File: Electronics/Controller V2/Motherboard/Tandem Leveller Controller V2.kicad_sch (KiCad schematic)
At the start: 6 parts, among them J8 776180-1, J9 776279-1

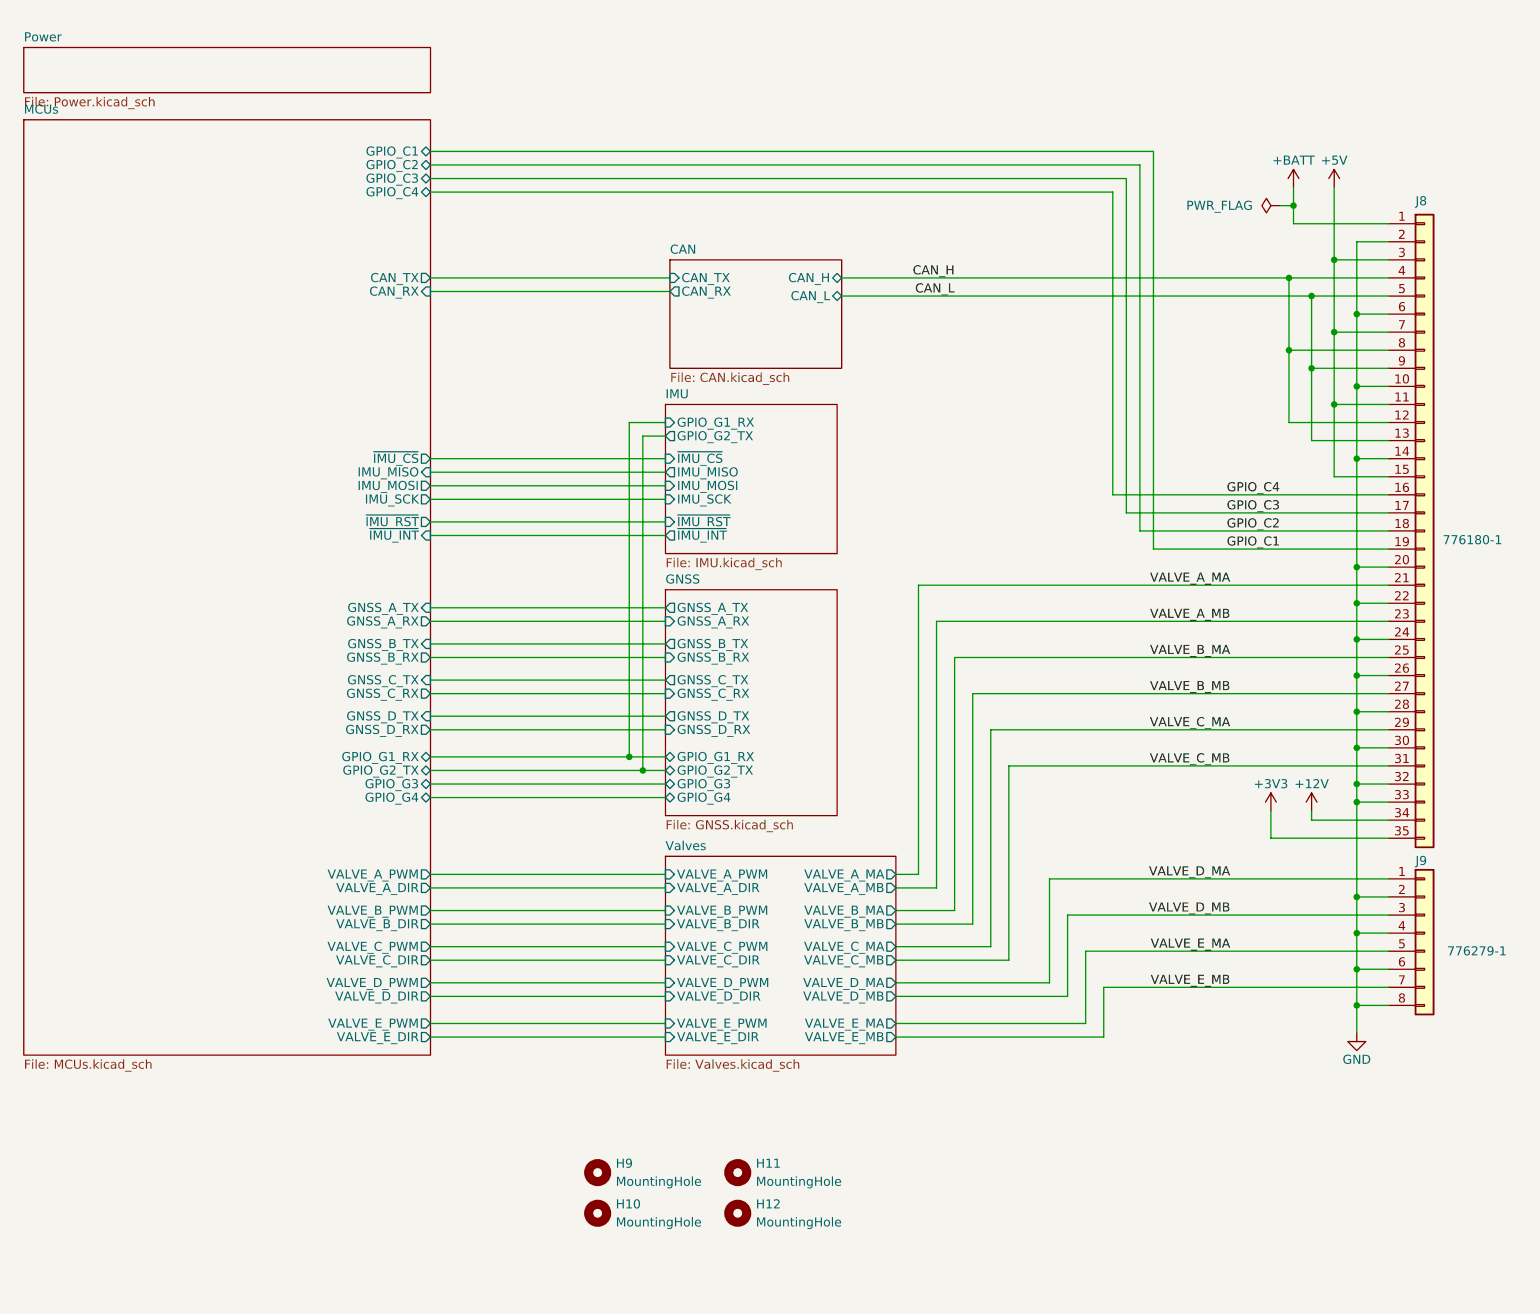
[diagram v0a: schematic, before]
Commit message: Added relay to control output of valve E.
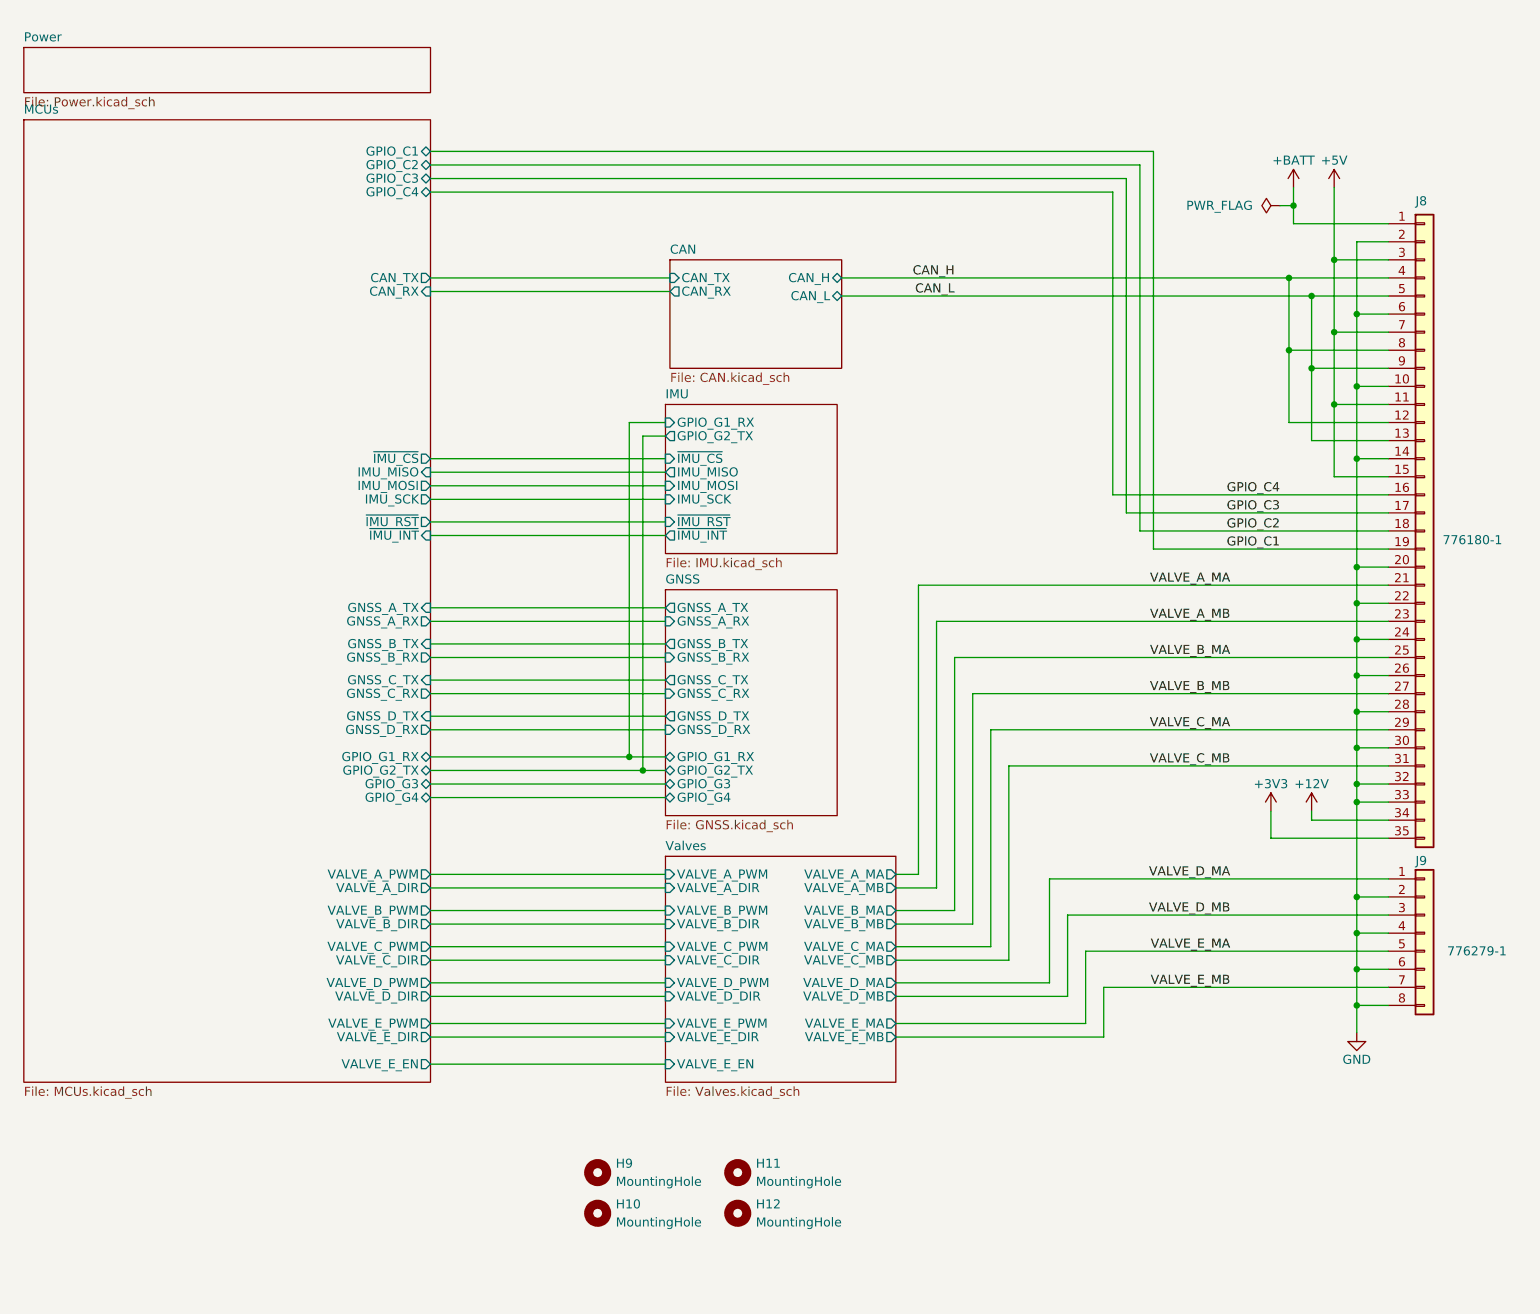
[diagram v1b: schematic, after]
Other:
- sheet MCUs ports: added VALVE_E_EN; removed none
- sheet Valves ports: added VALVE_E_EN; removed none
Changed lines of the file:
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@@
   (title_block
     (title "Tandem Leveller Controller")
-    (date "2026-02-09")
+    (date "2026-03-01")
     (rev "V2.0")
     (company "(C) andy@britishideas.com 2026")
@@
   )
   (wire (pts (xy 233.68 147.32) (xy 233.68 142.24))
+    (stroke (width 0) (type default))
+  )
+  (wire (pts (xy 103.505 160.655) (xy 136.525 160.655))
     (stroke (width 0) (type default))
   )
@@
     )
   )
-  (sheet (at 136.525 131.445) (size 32.385 27.94) (fields_autoplaced)
+  (sheet (at 136.525 131.445) (size 32.385 31.75) (fields_autoplaced)
     (stroke (width 0.1524) (type solid))
     (fill (color 0 0 0 0.0000))
@@
       (effects (font (size 1.27 1.27)) (justify left bottom))
     )
-    (property "Sheetfile" "Valves.kicad_sch" (at 136.525 159.9696 0)
+    (property "Sheetfile" "Valves.kicad_sch" (at 136.525 163.7796 0)
       (effects (font (size 1.27 1.27)) (justify left top))
     )
@@
     (pin "VALVE_A_MB" output (at 168.91 135.89 0)
       (effects (font (size 1.27 1.27)) (justify right))
+    )
+    (pin "VALVE_E_EN" input (at 136.525 160.655 180)
+      (effects (font (size 1.27 1.27)) (justify left))
     )
     (instances
@@
     )
   )
-  (sheet (at 46.355 27.94) (size 57.15 131.445) (fields_autoplaced)
+  (sheet (at 46.355 27.94) (size 57.15 135.255) (fields_autoplaced)
     (stroke (width 0.1524) (type solid))
     (fill (color 0 0 0 0.0000))
@@
       (effects (font (size 1.27 1.27)) (justify left bottom))
     )
-    (property "Sheetfile" "MCUs.kicad_sch" (at 46.355 159.9696 0)
+    (property "Sheetfile" "MCUs.kicad_sch" (at 46.355 163.7796 0)
       (effects (font (size 1.27 1.27)) (justify left top))
     )
@@
       (effects (font (size 1.27 1.27)) (justify right))
     )
+    (pin "VALVE_E_EN" output (at 103.505 160.655 0)
+      (effects (font (size 1.27 1.27)) (justify right))
+    )

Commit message: Working on autosteer support for V2 controller.
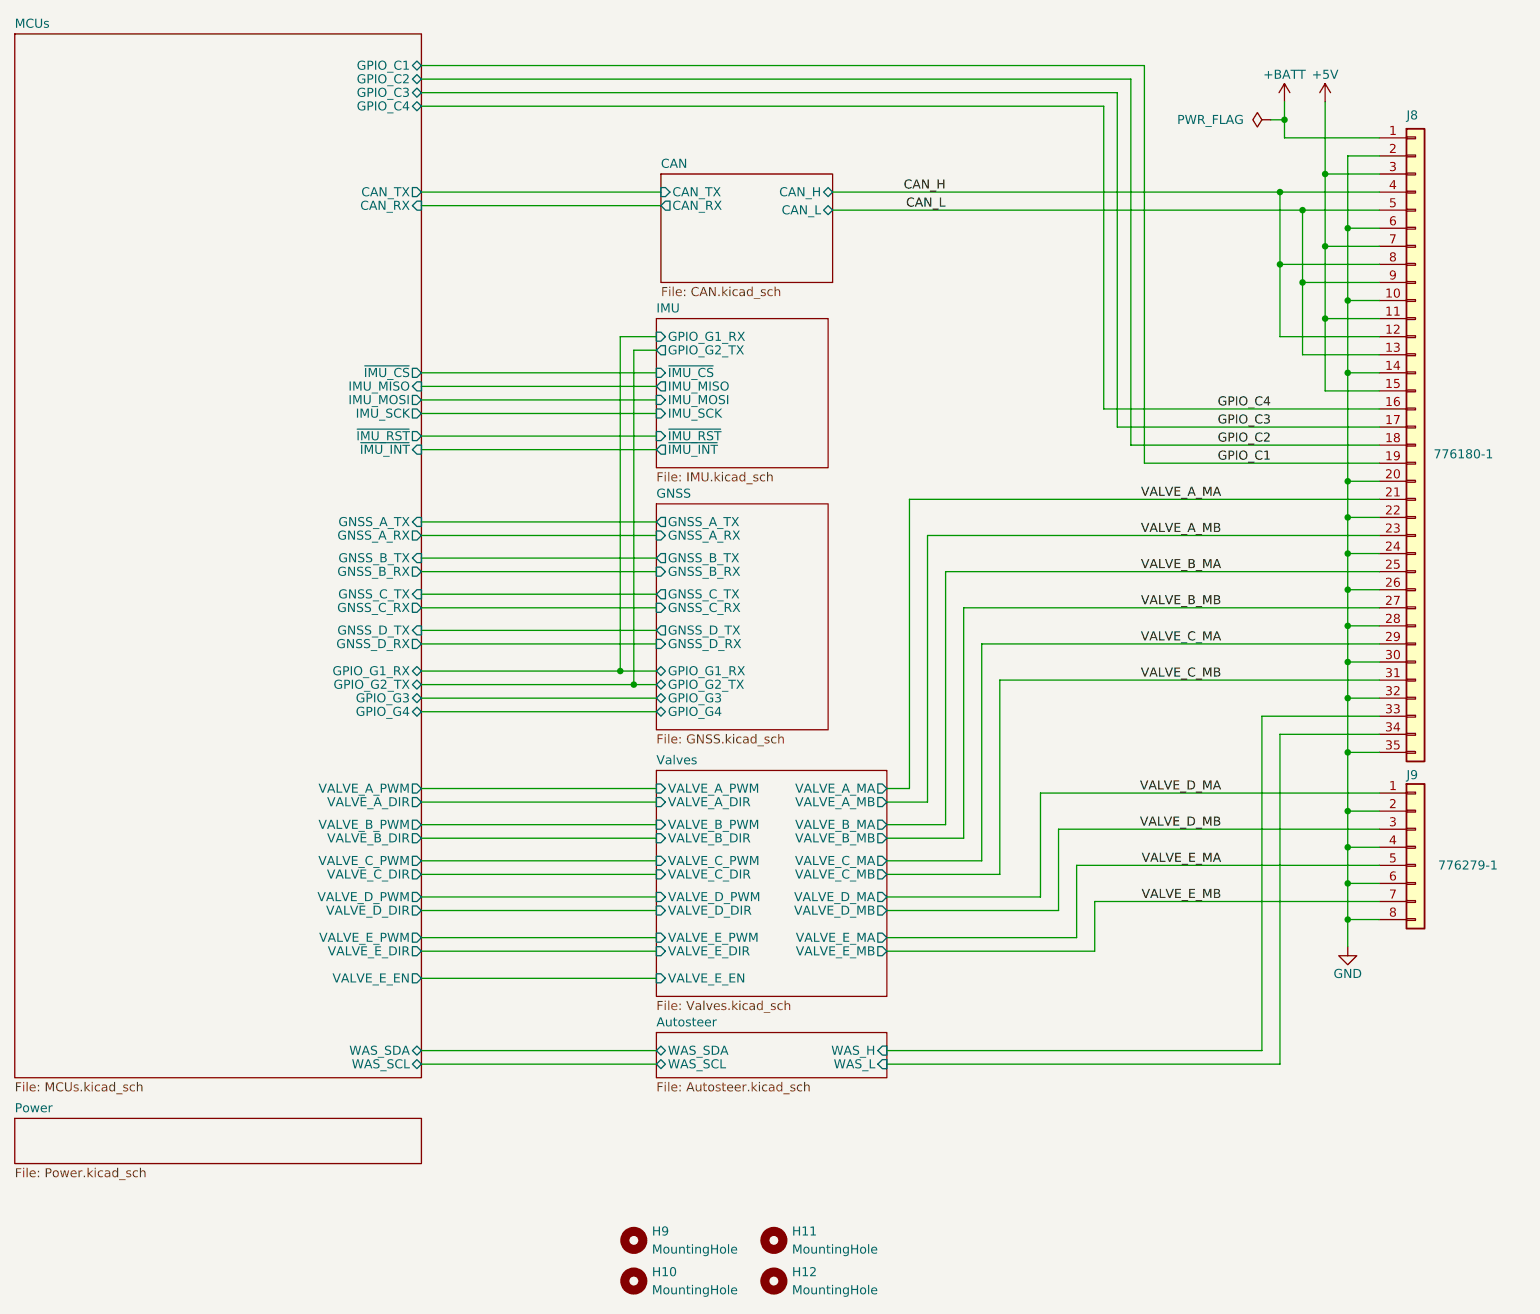
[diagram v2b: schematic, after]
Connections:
- net +3V3 is gone; now on net GND: J8.35 (Pin_35)
- net GND: no longer J8.33 (Pin_33)
- net +12V renamed Autosteer/WAS_L
- new net Autosteer/WAS_H: J8.33 (Pin_33)
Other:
- added sheet Autosteer (Autosteer.kicad_sch)
- sheet MCUs ports: added WAS_SCL, WAS_SDA; removed none
- moved on the sheet: H10, H11, H12, H9, J8, J9

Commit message: Added WAS circuit.
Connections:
- net GPIO_C4 is gone; now on net +5V: J8.16 (Pin_16)
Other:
- sheet MCUs ports: added none; removed GPIO_C4
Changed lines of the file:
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@@
   (junction (at 232.41 78.74) (diameter 0) (color 0 0 0 0)
   )
+  (junction (at 229.235 66.04) (diameter 0) (color 0 0 0 0)
+  )
   (junction (at 130.175 105.41) (diameter 0) (color 0 0 0 0)
   )
@@
     (stroke (width 0) (type default))
   )
-  (wire (pts (xy 198.12 26.035) (xy 198.12 68.58))
-    (stroke (width 0) (type default))
-  )
   (wire (pts (xy 232.41 63.5) (xy 236.855 63.5))
     (stroke (width 0) (type default))
@@
     (stroke (width 0) (type default))
   )
-  (wire (pts (xy 198.12 68.58) (xy 236.855 68.58))
-    (stroke (width 0) (type default))
-  )
   (wire (pts (xy 229.235 45.72) (xy 229.235 35.56))
     (stroke (width 0) (type default))
@@
     (stroke (width 0) (type default))
   )
-  (wire (pts (xy 102.235 26.035) (xy 198.12 26.035))
-    (stroke (width 0) (type default))
-  )
   (wire (pts (xy 236.855 55.88) (xy 229.235 55.88))
     (stroke (width 0) (type default))
@@
     (stroke (width 0) (type default))
   )
+  (wire (pts (xy 236.855 68.58) (xy 229.235 68.58))
+    (stroke (width 0) (type default))
+  )
   (wire (pts (xy 102.235 158.75) (xy 135.255 158.75))
     (stroke (width 0) (type default))
@@
     (stroke (width 0) (type default))
   )
+  (wire (pts (xy 229.235 68.58) (xy 229.235 66.04))
+    (stroke (width 0) (type default))
+  )
   (wire (pts (xy 102.235 121.92) (xy 135.255 121.92))
     (stroke (width 0) (type default))
@@
   )
   (label "VALVE_A_MA" (at 214.63 81.28 180) (fields_autoplaced)
-    (effects (font (size 1.27 1.27)) (justify right bottom))
-  )
-  (label "GPIO_C4" (at 221.615 68.58 180) (fields_autoplaced)
     (effects (font (size 1.27 1.27)) (justify right bottom))
   )
@@
       (effects (font (size 1.27 1.27)) (justify right))
     )
-    (pin "GPIO_C4" bidirectional (at 102.235 26.035 0)
-      (effects (font (size 1.27 1.27)) (justify right))
-    )
